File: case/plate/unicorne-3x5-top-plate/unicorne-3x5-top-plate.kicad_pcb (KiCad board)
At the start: 2 copper layers, 114.6 x 91.4 mm, 23 parts, among them SW1 SW_MX_HS, SW10 SW_MX_HS, SW11 SW_MX_HS, SW12 SW_MX_HS, SW13 SW_MX_HS, SW14 SW_MX_HS, SW15 SW_MX_HS, SW16 SW_MX_HS, SW17 SW_MX_HS, SW18 SW_MX_HS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

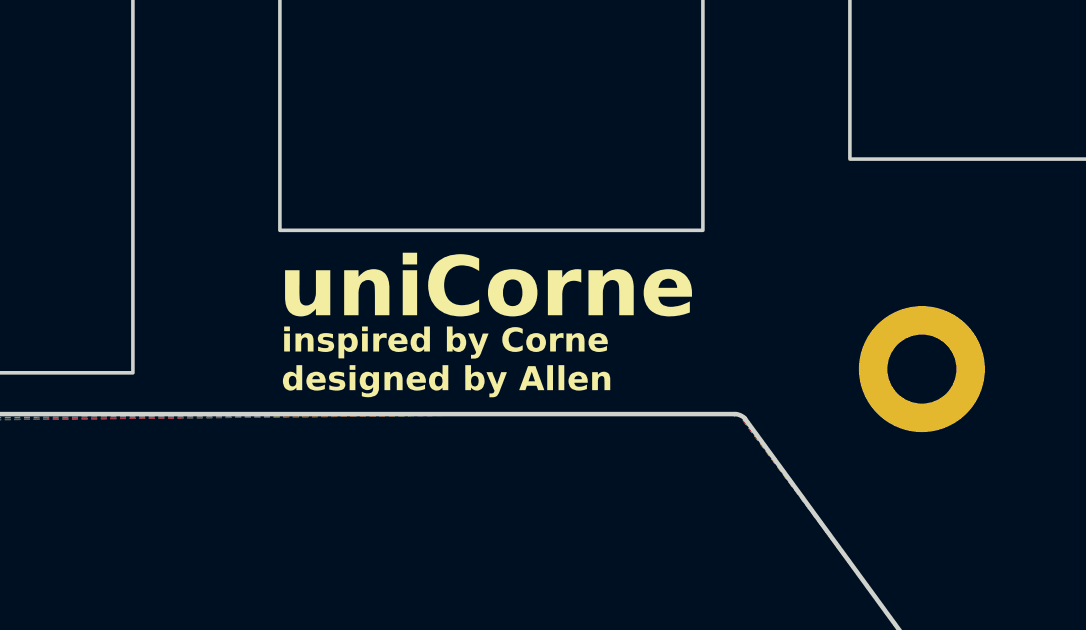
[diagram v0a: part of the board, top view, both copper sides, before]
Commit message: added plates
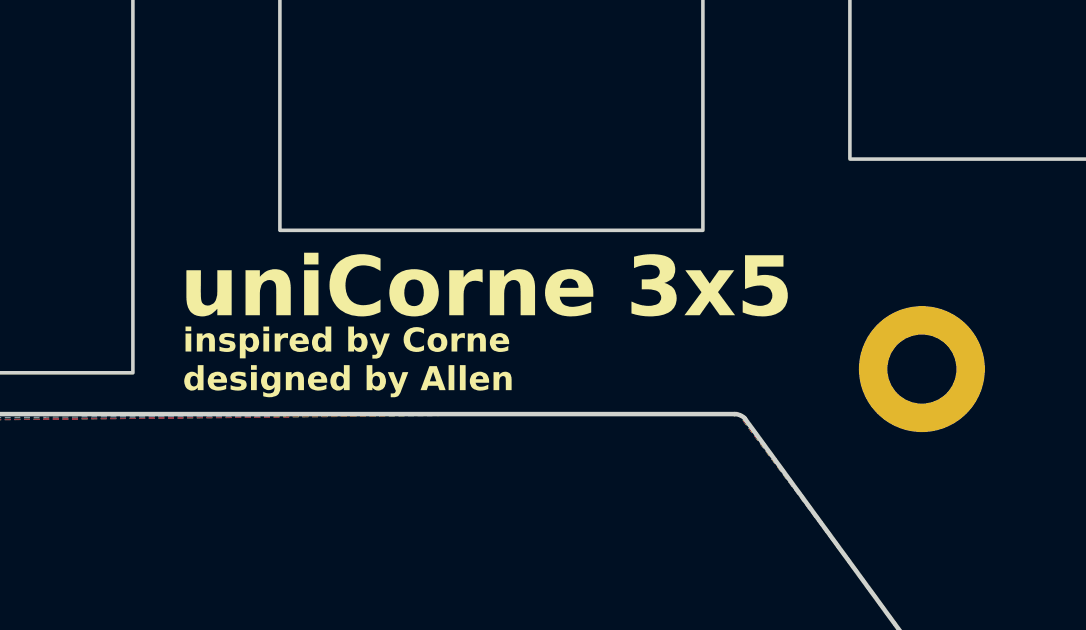
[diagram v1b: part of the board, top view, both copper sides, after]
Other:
- board text added: "uniCorne 3x5"
- board text removed: "uniCorne"
